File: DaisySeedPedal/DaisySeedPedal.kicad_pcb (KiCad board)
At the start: 2 copper layers, 41 parts, among them J1 Power, J2 GND, J3 Input, J4 Output, SW1 FS1, SW2 FS2, SW3 SW_SPDT, SW4 SW_SPDT, SW5 SW_SPDT, SW6 SW_SPDT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

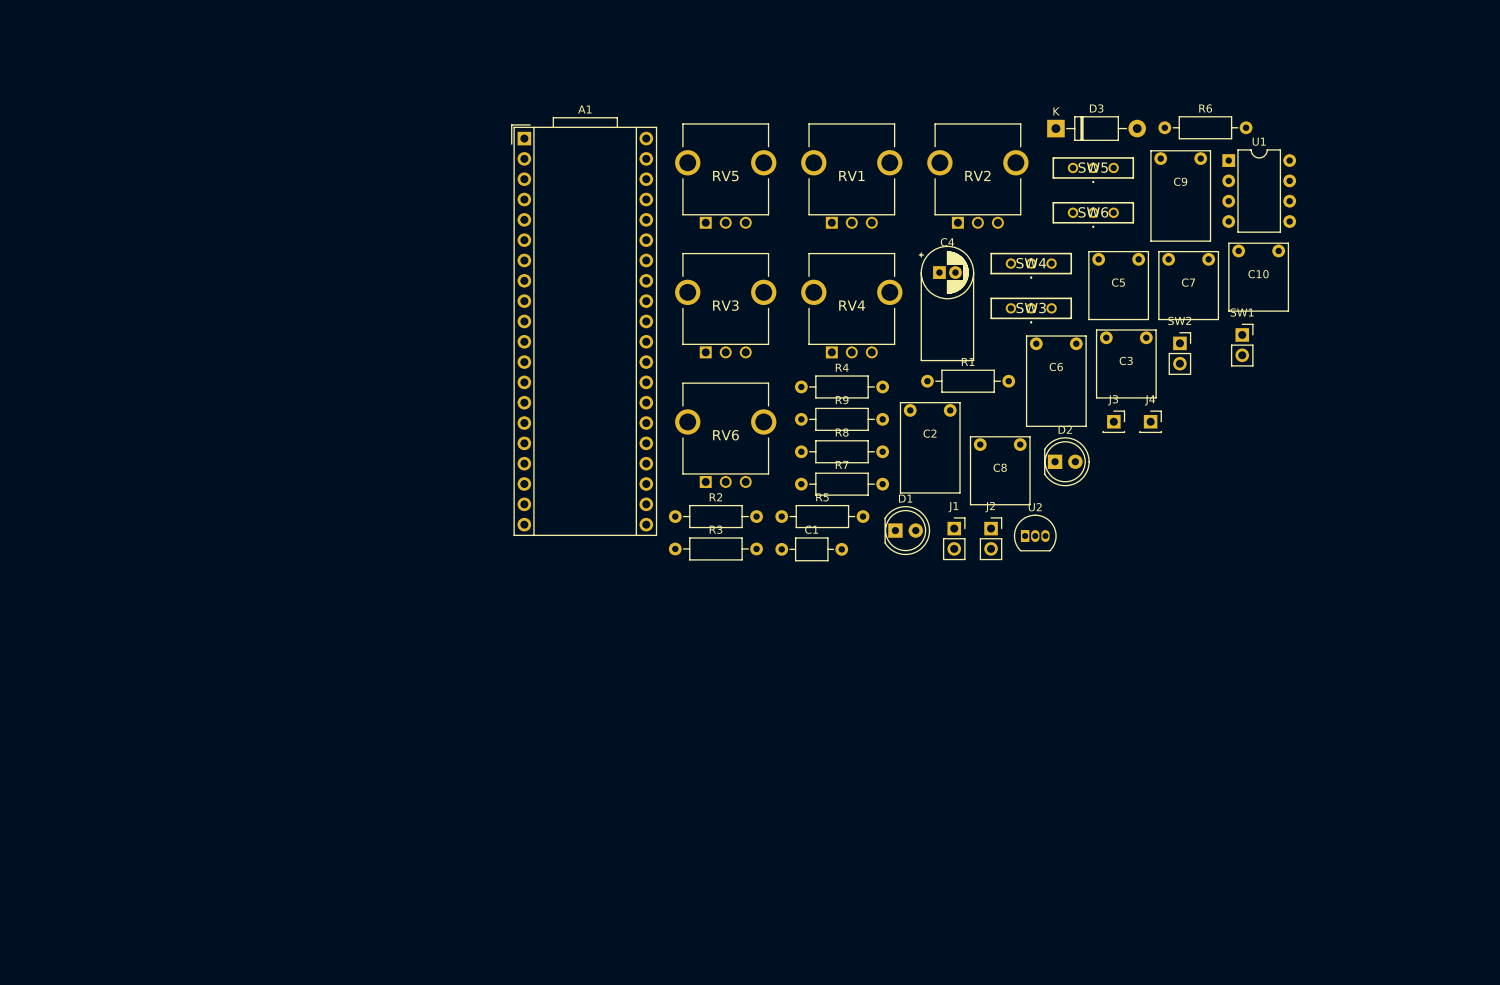
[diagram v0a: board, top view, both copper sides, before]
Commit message: Moved some footprints around
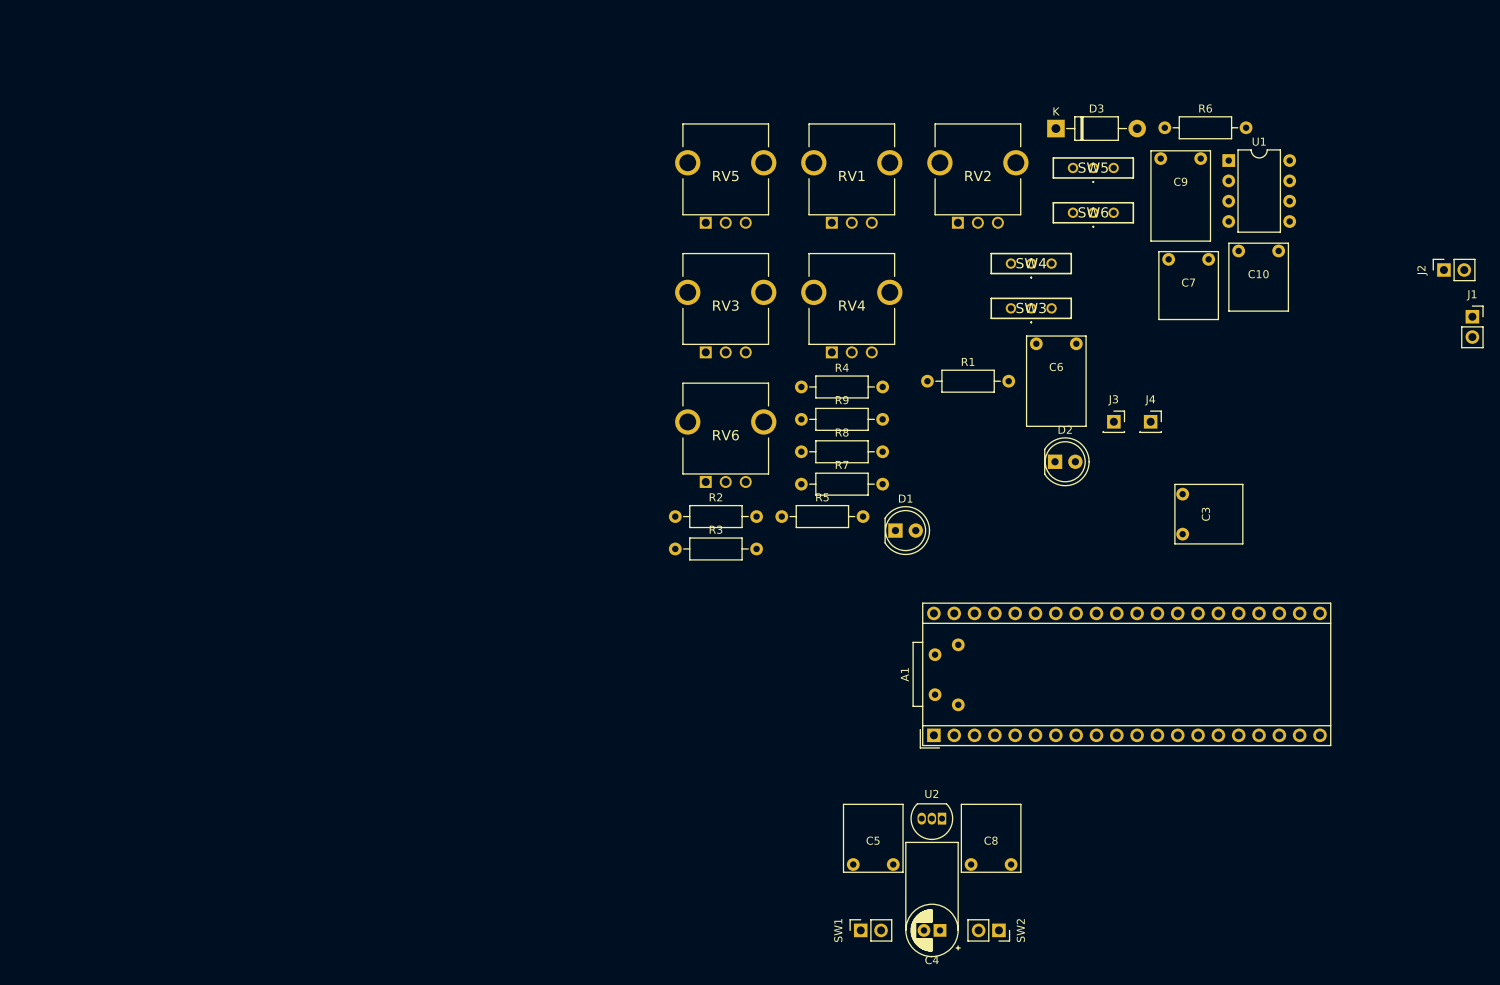
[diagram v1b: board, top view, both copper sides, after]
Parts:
- C1, C2: moved to B.Cu
- moved A1 90.5 mm to (153.9, 134.4), turned to 90 degrees
- moved SW1 88.4 mm to (144.8, 158.8), turned to 90 degrees
- moved C4 82.2 mm to (154.7, 158.8), turned to 180 degrees
- moved C5 79.1 mm to (148.8, 150.1), turned to 180 degrees
- moved SW2 76.8 mm to (162.1, 158.8), turned to 270 degrees
- moved J1 70.0 mm to (221.2, 82.0)
- moved J2 65.2 mm to (217.7, 76.2), turned to 90 degrees
- moved C8 51.8 mm to (163.6, 150.1), turned to 180 degrees
- moved U2 36.8 mm to (154.9, 144.8), turned to 180 degrees
- moved C2 35.2 mm to (153.7, 129.3), turned to 90 degrees
- moved C1 29.4 mm to (157.0, 130.6), turned to 90 degrees
- moved C3 26.1 mm to (185.4, 109.2), turned to 90 degrees

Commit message: Still placing components
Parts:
- C1, C2: moved to F.Cu
- RV1, RV2, RV3, RV4, RV5, RV6: footprint libraries:RK09L1140A65 -> libraries:R_POT
- U2: footprint Package_TO_SOT_THT:TO-92_Inline -> Package_TO_SOT_THT:TO-92_Inline_Wide
- moved J1 158.2 mm to (66.3, 50.0), turned to 270 degrees
- moved J2 134.0 mm to (86.2, 50.0), turned to 270 degrees
- moved J3 132.0 mm to (46.0, 74.9)
- moved C7 131.7 mm to (56.9, 112.3), turned to 180 degrees
- moved A1 121.2 mm to (51.2, 70.0)
- moved C3 120.7 mm to (64.8, 112.3), turned to 180 degrees
- moved U1 118.2 mm to (80.0, 103.9)
- moved SW3 111.6 mm to (55.0, 92.0), turned to 270 degrees
- moved C1 109.7 mm to (48.8, 112.8)
- moved C2 109.5 mm to (45.5, 112.3), turned to 180 degrees
- moved C10 107.2 mm to (85.3, 84.3), turned to 180 degrees
- moved D1 104.3 mm to (45.5, 120.7)
- moved SW1 104.3 mm to (45.5, 127.0)
- moved R6 103.9 mm to (89.9, 104.9)
- moved C5 103.0 mm to (69.6, 84.3)
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
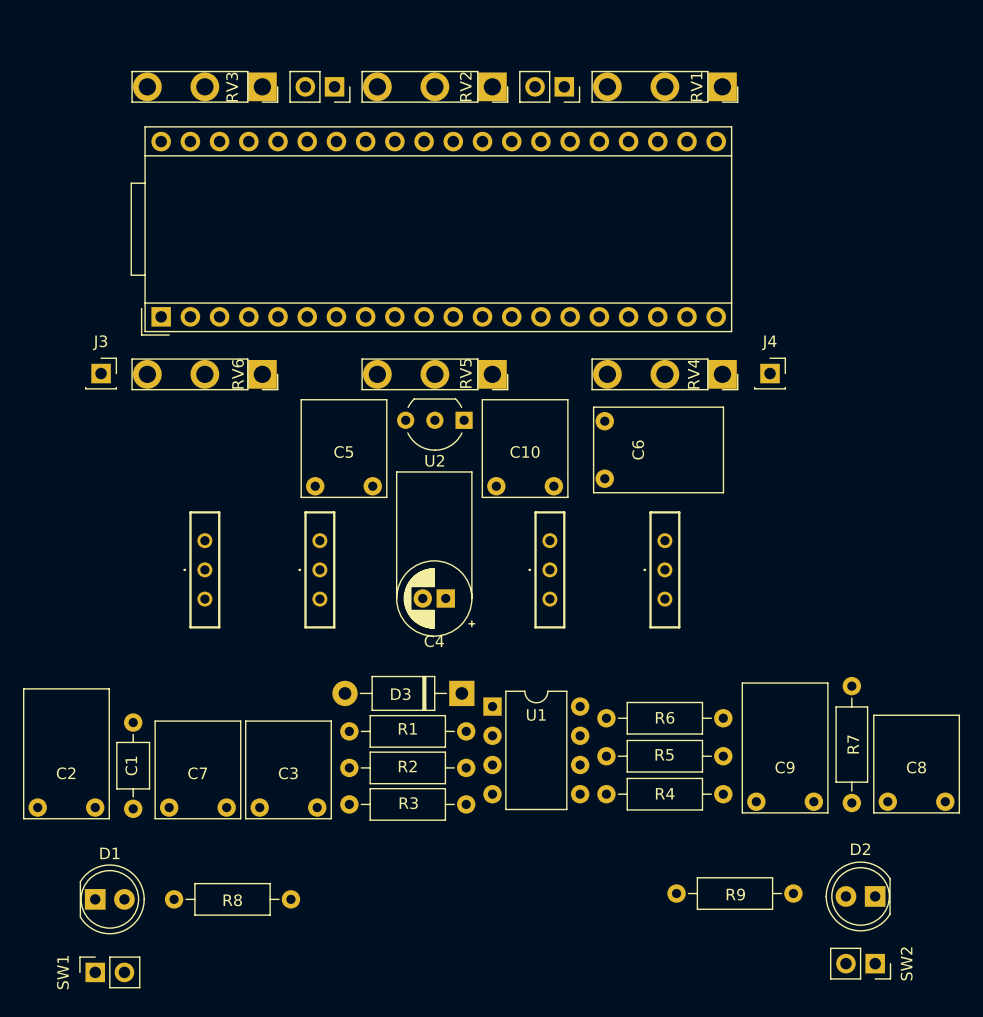
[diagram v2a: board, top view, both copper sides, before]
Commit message: Finalized board traces. Now working on silkscreen
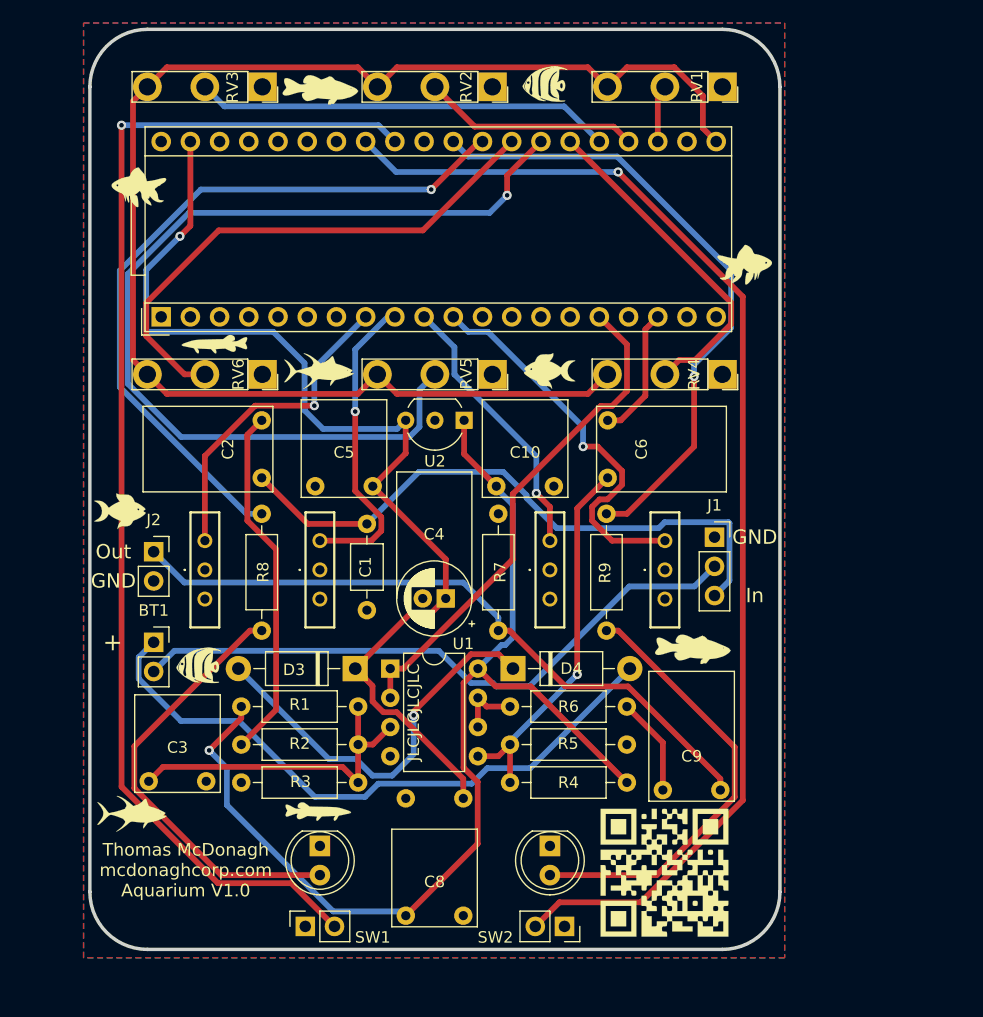
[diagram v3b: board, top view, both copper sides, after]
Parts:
- removed J3: Input, Connector_PinSocket_2.54mm:PinSocket_1x01_P2.54mm_Vertical
- removed J4: Output, Connector_PinSocket_2.54mm:PinSocket_1x01_P2.54mm_Vertical
- added BT1: Battery, Connector_PinSocket_2.54mm:PinSocket_1x02_P2.54mm_Vertical, F.Cu at (50.5, 98.3)
- added D4: D, Diode_THT:D_DO-41_SOD81_P10.16mm_Horizontal, F.Cu at (81.8, 100.6)
- added G***: LOGO, libraries:fish4, F.Cu at (48.9, 58.8)
- added G***: LOGO, libraries:fish2, F.Cu at (65.0, 50.3)
- added G***: LOGO, libraries:fish1, F.Cu at (84.6, 49.8)
- added G***: LOGO, libraries:fish1, F.Cu at (54.5, 100.3)
- added G***: LOGO, libraries:mcdonaghcorpQR, B.Cu at (95.0, 118.4)
- added G***: LOGO, libraries:mcdonaghcorpQR, F.Cu at (95.0, 118.4)
- added G***: LOGO, libraries:fish6, F.Cu at (58.4, 72.5)
- added G***: LOGO, libraries:fish3, F.Cu at (85.6, 74.8)
- added G***: LOGO, libraries:fish6, F.Cu at (64.9, 113.2)
- added G***: LOGO, libraries:fish5, F.Cu at (48.6, 113.2)
- added G***: LOGO, libraries:fish5, F.Cu at (64.9, 74.7)
- added G***: LOGO, libraries:fish4, F.Cu at (101.9, 65.5)
- added G***: LOGO, libraries:fish3, F.Cu at (47.8, 87.0)
- added G***: LOGO, libraries:fish2, F.Cu at (97.4, 98.9)
- C7: moved to B.Cu
- J1: value Power -> AudioJack3; footprint Connector_PinSocket_2.54mm:PinSocket_1x02_P2.54mm_Vertical -> Connector_PinSocket_2.54mm:PinSocket_1x03_P2.54mm_Vertical
- J2: value GND -> AudioJack2
- moved J2 53.9 mm to (50.5, 90.4), turned to 0 degrees
- moved J1 51.2 mm to (99.3, 89.2), turned to 0 degrees
- moved C8 43.1 mm to (77.5, 121.7)
- moved C2 36.1 mm to (59.5, 79.0), turned to 270 degrees
- moved R7 34.2 mm to (80.5, 97.3)
- moved R8 33.6 mm to (59.9, 87.1), turned to 270 degrees
- moved R9 33.6 mm to (89.9, 87.1), turned to 270 degrees
- moved D2 28.6 mm to (85.0, 116.0), turned to 270 degrees
- moved SW2 27.2 mm to (86.3, 123.0)
- moved C1 26.7 mm to (69.1, 95.5)
- moved C7 20.6 mm to (77.5, 112.3)
- moved D1 20.1 mm to (65.0, 116.0), turned to 270 degrees
- moved SW1 18.7 mm to (63.7, 123.0)
- moved C3 9.92 mm to (55.1, 110.0)
- moved R1 9.64 mm to (58.2, 103.9)
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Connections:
- J1 pad 1: +9V -> GND
- J1 pad 2: GND -> Net-(BT1-Pad2)
- J2 pad 1: GND -> /Output
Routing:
- net /3V3_A: track 0.00 -> 126.2 mm
- net /pin32: track 0.00 -> 105.4 mm, vias 0 -> 1
- net /pin33: track 0.00 -> 104.8 mm, vias 0 -> 1
- net Net-(C10-Pad2): track 0.00 -> 96.8 mm, vias 0 -> 1
- net /VIN: track 0.00 -> 92.4 mm, vias 0 -> 1
- net /pin27: track 0.00 -> 84.0 mm, vias 0 -> 1
- net /pin29: track 0.00 -> 63.2 mm, vias 0 -> 1
- net /Output: track 0.00 -> 59.1 mm
- net /pin30: track 0.00 -> 55.5 mm, vias 0 -> 1
- net Net-(BT1-Pad1): track 0.00 -> 55.3 mm
- net Net-(BT1-Pad2): track 0.00 -> 55.1 mm
- net /Input: track 0.00 -> 53.5 mm
- net /pin28: track 0.00 -> 46.9 mm
- net /pin16: track 0.00 -> 43.9 mm
- net Net-(D2-Pad2): track 0.00 -> 38.6 mm
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- added copper zone on B.Cu, net GND
- added copper zone on F.Cu, net GND
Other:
- board outline added: 60 x 80 mm
- board text added: "+"
- board text added: "GND"
- board text added: "In"
- board text added: "JLCJLCJLCJLC"
- board text added: "Out"
- board text added: "Thomas McDonagh mcdonaghcorp.com Aquarium V1.0"

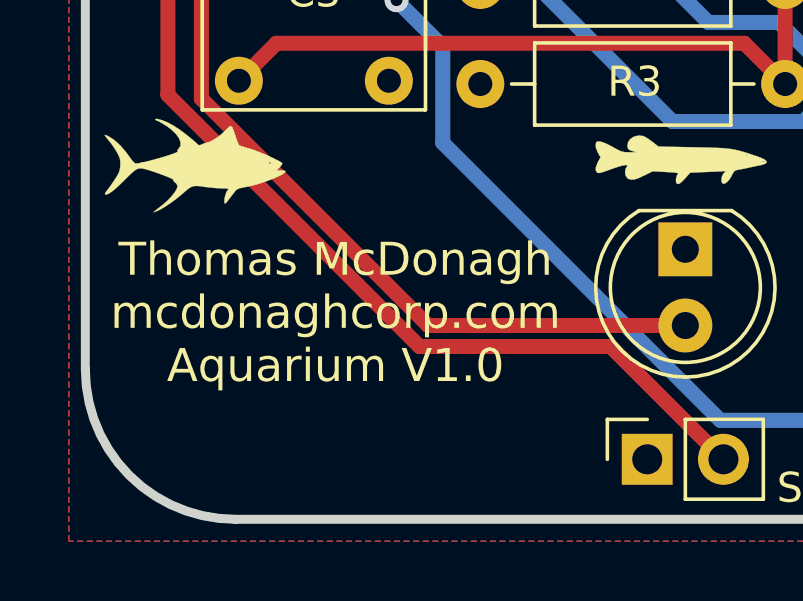
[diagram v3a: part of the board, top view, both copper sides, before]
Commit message: Finalized pcb and plotted gerbers
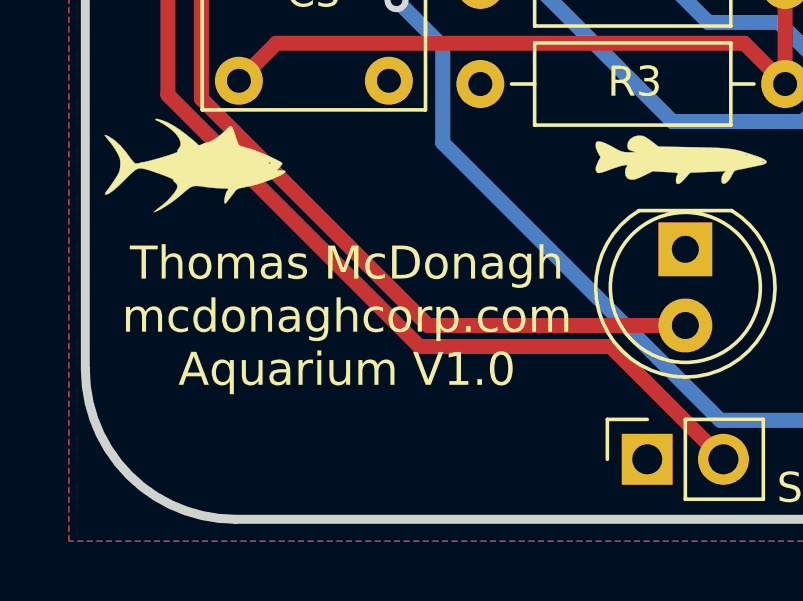
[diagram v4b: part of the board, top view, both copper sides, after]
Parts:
- added G***: LOGO, libraries:koiPondFish2, B.Cu at (68.2, 107.2)
- added G***: LOGO, libraries:koiPondFish1, B.Cu at (112.5, 120.4)
- added G***: LOGO, libraries:koiPondFish1, B.Cu at (47.2, 109.1)
- added G***: LOGO, libraries:koiPondFish1, B.Cu at (74.4, 117.7)
- added G***: LOGO, libraries:koiPondFish1, B.Cu at (90.9, 105.5)
- added G***: LOGO, libraries:koiPond, B.Cu at (75.2, 75.8)
